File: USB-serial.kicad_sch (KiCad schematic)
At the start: 14 parts

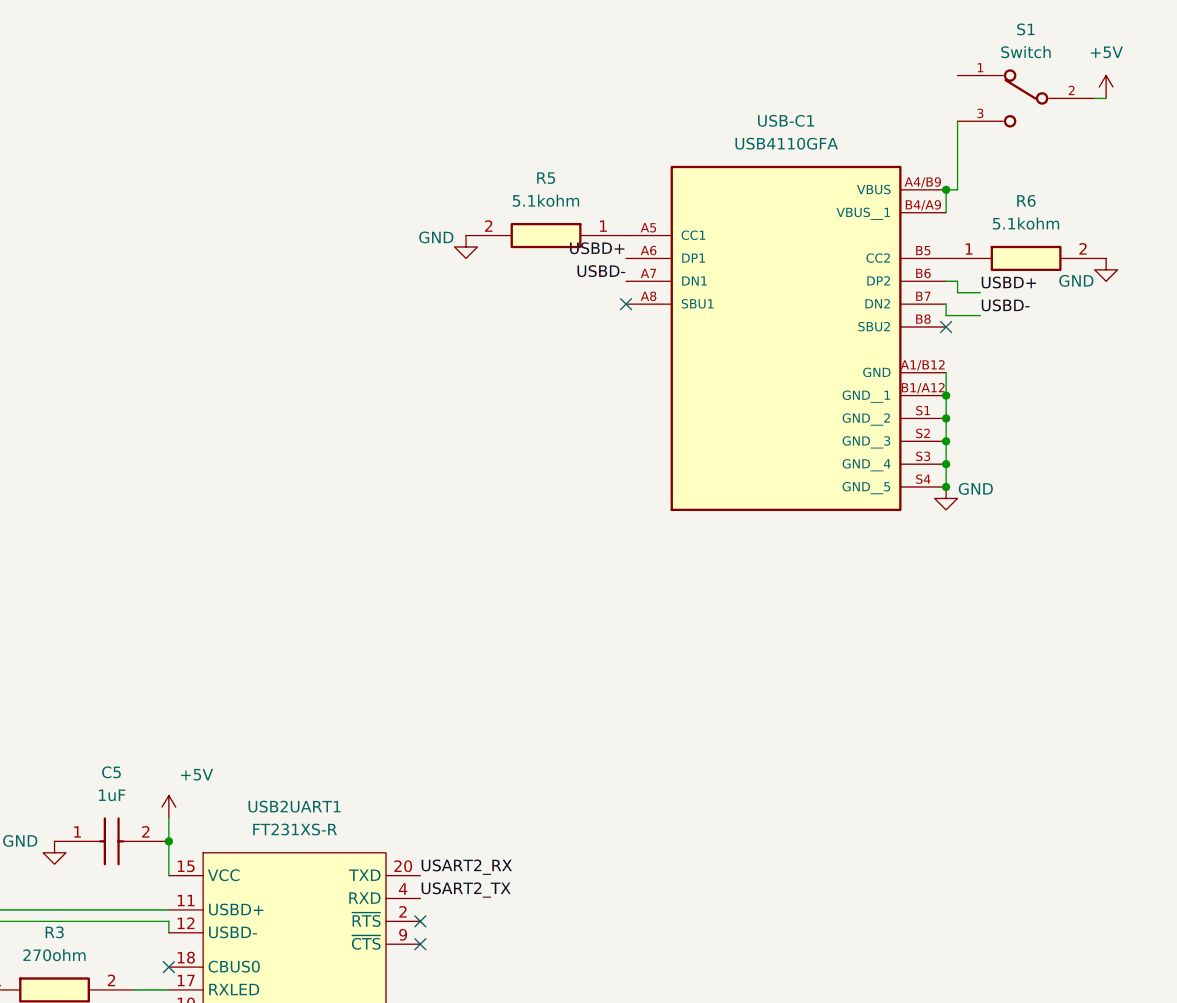
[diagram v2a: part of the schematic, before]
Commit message: standardize 5V and 3V3 labels
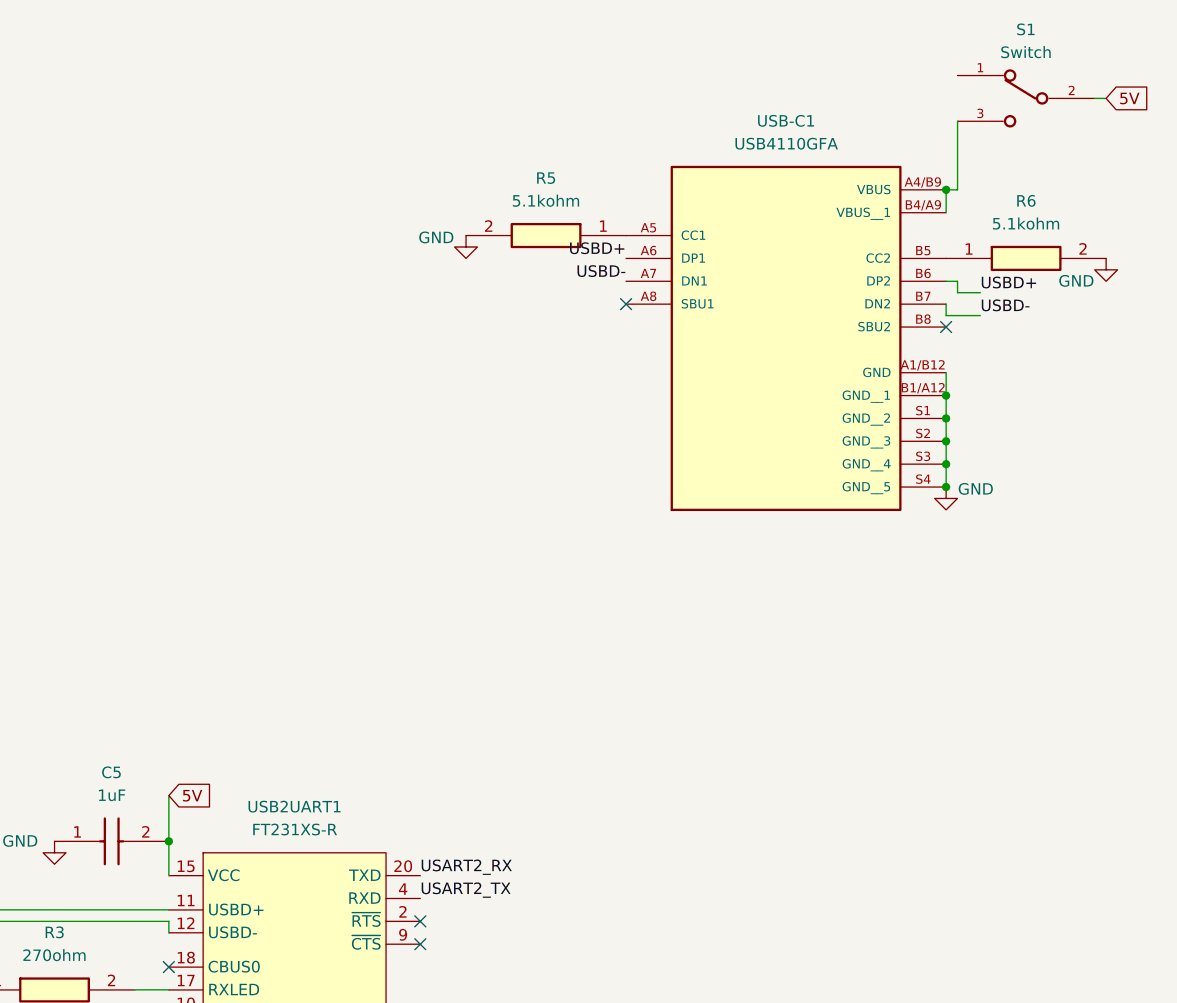
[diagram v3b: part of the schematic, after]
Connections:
- net +5V renamed 5V
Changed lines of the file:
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@@
 	(wire
 		(pts
-			(xy 102.87 139.7) (xy 102.87 142.24)
+			(xy 102.87 137.16) (xy 102.87 142.24)
 		)
 		(stroke
@@
 			)
 			(justify right bottom)
+		)
+	)
+	(global_label "5V"
+		(shape input)
+		(at 102.87 137.16 0)
+		(fields_autoplaced yes)
+		(effects
+			(font
+				(size 1.27 1.27)
+			)
+			(justify left)
+		)
+		(property "Intersheetrefs" "${INTERSHEET_REFS}"
+			(at 108.1533 137.16 0)
+			(effects
+				(font
+					(size 1.27 1.27)
+				)
+				(justify left)
+				(hide yes)
+			)
+		)
+	)
+	(global_label "5V"
+		(shape input)
+		(at 207.01 59.69 0)
+		(fields_autoplaced yes)
+		(effects
+			(font
+				(size 1.27 1.27)
+			)
+			(justify left)
+		)
+		(property "Intersheetrefs" "${INTERSHEET_REFS}"
+			(at 212.2933 59.69 0)
+			(effects
+				(font
+					(size 1.27 1.27)
+				)
+				(justify left)
+				(hide yes)
+			)
 		)
 	)
@@
 	)
 	(symbol
-		(lib_id "power:+5V")
-		(at 207.01 59.69 0)
-		(mirror y)
-		(unit 1)
-		(exclude_from_sim no)
-		(in_bom yes)
-		(on_board yes)
-		(dnp no)
-		(property "Reference" "#PWR012"
-			(at 207.01 63.5 0)
-			(effects
-				(font
-					(size 1.27 1.27)
-				)
-				(hide yes)
-			)
-		)
-		(property "Value" "+5V"
-			(at 207.01 54.61 0)
-			(effects
-				(font
-					(size 1.27 1.27)
-				)
-			)
-		)
-		(property "Footprint" ""
-			(at 207.01 59.69 0)
-			(effects
-				(font
-					(size 1.27 1.27)
-				)
-				(hide yes)
-			)
-		)
-		(property "Datasheet" ""
-			(at 207.01 59.69 0)
-			(effects
-				(font
-					(size 1.27 1.27)
-				)
-				(hide yes)
-			)
-		)
-		(property "Description" "Power symbol creates a global label with name \"+5V\""
-			(at 207.01 59.69 0)
-			(effects
-				(font
-					(size 1.27 1.27)
-				)
-				(hide yes)
-			)
-		)
-		(pin "1"
-		)
-		(instances
-			(project "harm_drone"
-				(path "/5ce3566e-4e0f-420e-9b0d-3952cd3c63fd/8f41fec2-6210-43dd-9328-85befbc13075"
-					(reference "#PWR012")
-					(unit 1)
-				)
-			)
-		)
-	)
-	(symbol
 		(lib_id "power:GND")
 		(at 207.01 77.47 0)
@@
 					(unit 1)
 				)
-			)
-		)
-	)
-	(symbol
-		(lib_id "power:+5V")
-		(at 102.87 139.7 0)
-		(mirror y)
-		(unit 1)
-		(exclude_from_sim no)
-		(in_bom yes)
-		(on_board yes)
-		(dnp no)
-		(property "Reference" "#PWR09"
-			(at 102.87 143.51 0)
-			(effects
-				(font
-					(size 1.27 1.27)
-				)
-				(hide yes)
-			)
-		)
-		(property "Value" "+5V"
-			(at 105.918 134.874 0)
-			(effects
-				(font
-					(size 1.27 1.27)
-				)
-			)
-		)
-		(property "Footprint" ""
-			(at 102.87 139.7 0)
-			(effects
-				(font
-					(size 1.27 1.27)
-				)
-				(hide yes)
-			)
-		)
-		(property "Datasheet" ""
-			(at 102.87 139.7 0)
-			(effects
-				(font
-					(size 1.27 1.27)
-				)
-				(hide yes)
-			)
-		)
-		(property "Description" "Power symbol creates a global label with name \"+5V\""
-			(at 102.87 139.7 0)
-			(effects
-				(font
-					(size 1.27 1.27)
-				)
-				(hide yes)
-			)
-		)
-		(pin "1"
-		)
-		(instances
-			(project "harm_drone"
-				(path "/5ce3566e-4e0f-420e-9b0d-3952cd3c63fd/8f41fec2-6210-43dd-9328-85befbc13075"
-					(reference "#PWR09")
-					(unit 1)
-				)

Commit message: finished up schematic
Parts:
- renumbered C3 to C12, C4 to C13, C5 to C14, R1 to R10, R2 to R11, R3 to R12, R4 to R13, R5 to R14, R6 to R15, S1 to S2
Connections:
- net USART2_RX renamed TXD_USB2SERIAL
- net USART2_TX renamed RXD_USB2SERIAL
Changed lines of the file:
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@@
+	(wire
+		(pts
+			(xy 134.62 146.05) (xy 130.81 146.05)
+		)
+		(stroke
+			(width 0)
+			(type default)
+		)
+	)
 	(wire
 		(pts
@@
 		(pts
 			(xy 193.04 83.82) (xy 189.23 83.82)
+		)
+		(stroke
+			(width 0)
+			(type default)
+		)
+	)
+	(wire
+		(pts
+			(xy 133.35 148.59) (xy 130.81 148.59)
 		)
 		(stroke
@@
 		)
 	)
-	(label "USART2_RX"
-		(at 130.81 146.05 0)
-		(fields_autoplaced yes)
-		(effects
-			(font
-				(size 1.27 1.27)
-			)
-			(justify left bottom)
-		)
-	)
 	(label "USBD-"
 		(at 153.67 80.01 180)
@@
 		)
 	)
-	(label "USART2_TX"
-		(at 130.81 148.59 0)
-		(fields_autoplaced yes)
-		(effects
-			(font
-				(size 1.27 1.27)
-			)
-			(justify left bottom)
-		)
-	)
 	(label "VCCIO"
 		(at 133.35 165.1 0)
@@
 			)
 			(justify right bottom)
+		)
+	)
+	(global_label "RXD_USB2SERIAL"
+		(shape input)
+		(at 133.35 148.59 0)
+		(effects
+			(font
+				(size 1.27 1.27)
+			)
+			(justify left)
+		)
+		(property "Intersheetrefs" "${INTERSHEET_REFS}"
+			(at 133.35 148.59 0)
+			(effects
+				(font
+					(size 1.27 1.27)
+				)
+				(hide yes)
+			)
+		)
+	)
+	(global_label "TXD_USB2SERIAL"
+		(shape output)
+		(at 134.62 146.05 0)
+		(effects
+			(font
+				(size 1.27 1.27)
+			)
+			(justify left)
+		)
+		(property "Intersheetrefs" "${INTERSHEET_REFS}"
+			(at 134.62 146.05 0)
+			(effects
+				(font
+					(size 1.27 1.27)
+				)
+				(hide yes)
+			)
 		)
 	)
@@
 		(on_board yes)
 		(dnp no)
-		(property "Reference" "#PWR08"
+		(property "Reference" "#PWR029"
 			(at 90.17 148.59 0)
 			(effects
@@
 			(project "harm_drone"
 				(path "/5ce3566e-4e0f-420e-9b0d-3952cd3c63fd/8f41fec2-6210-43dd-9328-85befbc13075"
-					(reference "#PWR08")
+					(reference "#PWR029")
 					(unit 1)
 				)
@@
 		(dnp no)
 		(fields_autoplaced yes)
-		(property "Reference" "R4"
+		(property "Reference" "R13"
 			(at 90.17 168.91 0)
 			(effects
@@
 			(project "harm_drone"
 				(path "/5ce3566e-4e0f-420e-9b0d-3952cd3c63fd/8f41fec2-6210-43dd-9328-85befbc13075"
-					(reference "R4")
+					(reference "R13")
 					(unit 1)
 				)
@@
 		(dnp no)
 		(fields_autoplaced yes)
-		(property "Reference" "S1"
+		(property "Reference" "S2"
 			(at 198.12 52.07 0)
 			(effects
@@
 			(project ""
 				(path "/5ce3566e-4e0f-420e-9b0d-3952cd3c63fd/8f41fec2-6210-43dd-9328-85befbc13075"
-					(reference "S1")
+					(reference "S2")
 					(unit 1)
 				)
@@
 		(dnp no)
 		(fields_autoplaced yes)
-		(property "Reference" "C5"
+		(property "Reference" "C14"
 			(at 96.52 134.62 0)
 			(effects
@@
 			(project "harm_drone"
 				(path "/5ce3566e-4e0f-420e-9b0d-3952cd3c63fd/8f41fec2-6210-43dd-9328-85befbc13075"
-					(reference "C5")
+					(reference "C14")
 					(unit 1)
 				)
@@
 		(on_board yes)
 		(dnp no)
-		(property "Reference" "#PWR013"
+		(property "Reference" "#PWR032"
 			(at 189.23 109.22 0)
 			(effects
@@
 			(project "harm_drone"
 				(path "/5ce3566e-4e0f-420e-9b0d-3952cd3c63fd/8f41fec2-6210-43dd-9328-85befbc13075"
-					(reference "#PWR013")
+					(reference "#PWR032")
 					(unit 1)
 				)
@@
 		(on_board yes)
 		(dnp no)
-		(property "Reference" "#PWR010"
+		(property "Reference" "#PWR031"
 			(at 135.89 81.28 0)
 			(effects
@@
 			(project "harm_drone"
 				(path "/5ce3566e-4e0f-420e-9b0d-3952cd3c63fd/8f41fec2-6210-43dd-9328-85befbc13075"
-					(reference "#PWR010")
+					(reference "#PWR031")
 					(unit 1)
 				)
@@
 		(on_board yes)
 		(dnp no)
-		(property "Reference" "#PWR06"
+		(property "Reference" "#PWR027"
 			(at 50.8 156.21 0)
 			(effects
@@
 			(project "harm_drone"
 				(path "/5ce3566e-4e0f-420e-9b0d-3952cd3c63fd/8f41fec2-6210-43dd-9328-85befbc13075"
-					(reference "#PWR06")
+					(reference "#PWR027")
 					(unit 1)
 				)
@@
 		(dnp no)
 		(fields_autoplaced yes)
-		(property "Reference" "R6"
+		(property "Reference" "R15"
 			(at 198.12 71.12 0)
 			(effects
@@
 			(project "harm_drone"
 				(path "/5ce3566e-4e0f-420e-9b0d-3952cd3c63fd/8f41fec2-6210-43dd-9328-85befbc13075"
-					(reference "R6")
+					(reference "R15")
 					(unit 1)
 				)
@@
 		(on_board yes)
 		(dnp no)
-		(property "Reference" "#PWR011"
+		(property "Reference" "#PWR030"
 			(at 130.81 184.15 0)
 			(effects
@@
 			(project "harm_drone"
 				(path "/5ce3566e-4e0f-420e-9b0d-3952cd3c63fd/8f41fec2-6210-43dd-9328-85befbc13075"
-					(reference "#PWR011")
+					(reference "#PWR030")
 					(unit 1)
 				)
@@
 		(dnp no)
 		(fields_autoplaced yes)
-		(property "Reference" "R2"
+		(property "Reference" "R11"
 			(at 71.12 128.27 0)
 			(effects
@@
 			(project "harm_drone"
 				(path "/5ce3566e-4e0f-420e-9b0d-3952cd3c63fd/8f41fec2-6210-43dd-9328-85befbc13075"
-					(reference "R2")
+					(reference "R11")
 					(unit 1)
 				)
@@
 		(dnp no)
 		(fields_autoplaced yes)
-		(property "Reference" "R1"
+		(property "Reference" "R10"
 			(at 69.85 139.7 0)
 			(effects
@@
 			(project "harm_drone"
 				(path "/5ce3566e-4e0f-420e-9b0d-3952cd3c63fd/8f41fec2-6210-43dd-9328-85befbc13075"
-					(reference "R1")
+					(reference "R10")
 					(unit 1)
 				)
@@
 		(on_board yes)
 		(dnp no)
-		(property "Reference" "#PWR014"
+		(property "Reference" "#PWR033"
 			(at 207.01 83.82 0)
 			(effects
@@
 			(project "harm_drone"
 				(path "/5ce3566e-4e0f-420e-9b0d-3952cd3c63fd/8f41fec2-6210-43dd-9328-85befbc13075"
-					(reference "#PWR014")
+					(reference "#PWR033")
 					(unit 1)
 				)
@@
 		(dnp no)
 		(fields_autoplaced yes)
-		(property "Reference" "R3"
+		(property "Reference" "R12"
 			(at 90.17 152.4 0)
 			(effects
@@
 			(project "harm_drone"
 				(path "/5ce3566e-4e0f-420e-9b0d-3952cd3c63fd/8f41fec2-6210-43dd-9328-85befbc13075"
-					(reference "R3")
+					(reference "R12")
 					(unit 1)
 				)
@@
 		(dnp no)
 		(fields_autoplaced yes)
-		(property "Reference" "C3"
+		(property "Reference" "C12"
 			(at 54.61 142.2399 90)
 			(effects
@@
 			(project "harm_drone"
 				(path "/5ce3566e-4e0f-420e-9b0d-3952cd3c63fd/8f41fec2-6210-43dd-9328-85befbc13075"
-					(reference "C3")
+					(reference "C12")
 					(unit 1)
 				)
@@
 		(dnp no)
 		(fields_autoplaced yes)
-		(property "Reference" "R5"
+		(property "Reference" "R14"
 			(at 144.78 68.58 0)
 			(effects
@@
 			(project "harm_drone"
 				(path "/5ce3566e-4e0f-420e-9b0d-3952cd3c63fd/8f41fec2-6210-43dd-9328-85befbc13075"
-					(reference "R5")
+					(reference "R14")
 					(unit 1)
 				)
@@
 		(dnp no)
 		(fields_autoplaced yes)
-		(property "Reference" "C4"
+		(property "Reference" "C13"
 			(at 55.88 126.9999 90)
 			(effects
@@
 			(project "harm_drone"
 				(path "/5ce3566e-4e0f-420e-9b0d-3952cd3c63fd/8f41fec2-6210-43dd-9328-85befbc13075"
-					(reference "C4")
+					(reference "C13")
 					(unit 1)
 				)
@@
 		(on_board yes)
 		(dnp no)
-		(property "Reference" "#PWR07"
+		(property "Reference" "#PWR028"
 			(at 52.07 115.57 0)
 			(effects
@@
 			(project "harm_drone"
 				(path "/5ce3566e-4e0f-420e-9b0d-3952cd3c63fd/8f41fec2-6210-43dd-9328-85befbc13075"
-					(reference "#PWR07")
+					(reference "#PWR028")
 					(unit 1)
 				)

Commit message: final changes
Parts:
- renumbered C12 to C27, C13 to C28, C14 to C29, R10 to R25, R11 to R26, R12 to R27, R13 to R28, R14 to R29, R15 to R30
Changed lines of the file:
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@@
 		(on_board yes)
 		(dnp no)
-		(property "Reference" "#PWR029"
+		(property "Reference" "#PWR034"
 			(at 90.17 148.59 0)
 			(effects
@@
 			(project "harm_drone"
 				(path "/5ce3566e-4e0f-420e-9b0d-3952cd3c63fd/8f41fec2-6210-43dd-9328-85befbc13075"
-					(reference "#PWR029")
+					(reference "#PWR034")
 					(unit 1)
 				)
@@
 		(dnp no)
 		(fields_autoplaced yes)
-		(property "Reference" "R13"
+		(property "Reference" "R28"
 			(at 90.17 168.91 0)
 			(effects
@@
 			(project "harm_drone"
 				(path "/5ce3566e-4e0f-420e-9b0d-3952cd3c63fd/8f41fec2-6210-43dd-9328-85befbc13075"
-					(reference "R13")
+					(reference "R28")
 					(unit 1)
 				)
@@
 		(dnp no)
 		(fields_autoplaced yes)
-		(property "Reference" "C14"
+		(property "Reference" "C29"
 			(at 96.52 134.62 0)
 			(effects
@@
 			(project "harm_drone"
 				(path "/5ce3566e-4e0f-420e-9b0d-3952cd3c63fd/8f41fec2-6210-43dd-9328-85befbc13075"
-					(reference "C14")
+					(reference "C29")
 					(unit 1)
 				)
@@
 		(on_board yes)
 		(dnp no)
-		(property "Reference" "#PWR032"
+		(property "Reference" "#PWR037"
 			(at 189.23 109.22 0)
 			(effects
@@
 			(project "harm_drone"
 				(path "/5ce3566e-4e0f-420e-9b0d-3952cd3c63fd/8f41fec2-6210-43dd-9328-85befbc13075"
-					(reference "#PWR032")
+					(reference "#PWR037")
 					(unit 1)
 				)
@@
 		(on_board yes)
 		(dnp no)
-		(property "Reference" "#PWR031"
+		(property "Reference" "#PWR036"
 			(at 135.89 81.28 0)
 			(effects
@@
 			(project "harm_drone"
 				(path "/5ce3566e-4e0f-420e-9b0d-3952cd3c63fd/8f41fec2-6210-43dd-9328-85befbc13075"
-					(reference "#PWR031")
+					(reference "#PWR036")
 					(unit 1)
 				)
@@
 		(on_board yes)
 		(dnp no)
-		(property "Reference" "#PWR027"
+		(property "Reference" "#PWR032"
 			(at 50.8 156.21 0)
 			(effects
@@
 			(project "harm_drone"
 				(path "/5ce3566e-4e0f-420e-9b0d-3952cd3c63fd/8f41fec2-6210-43dd-9328-85befbc13075"
-					(reference "#PWR027")
+					(reference "#PWR032")
 					(unit 1)
 				)
@@
 		(dnp no)
 		(fields_autoplaced yes)
-		(property "Reference" "R15"
+		(property "Reference" "R30"
 			(at 198.12 71.12 0)
 			(effects
@@
 			(project "harm_drone"
 				(path "/5ce3566e-4e0f-420e-9b0d-3952cd3c63fd/8f41fec2-6210-43dd-9328-85befbc13075"
-					(reference "R15")
+					(reference "R30")
 					(unit 1)
 				)
@@
 		(on_board yes)
 		(dnp no)
-		(property "Reference" "#PWR030"
+		(property "Reference" "#PWR035"
 			(at 130.81 184.15 0)
 			(effects
@@
 			(project "harm_drone"
 				(path "/5ce3566e-4e0f-420e-9b0d-3952cd3c63fd/8f41fec2-6210-43dd-9328-85befbc13075"
-					(reference "#PWR030")
+					(reference "#PWR035")
 					(unit 1)
 				)
@@
 		(dnp no)
 		(fields_autoplaced yes)
-		(property "Reference" "R11"
+		(property "Reference" "R26"
 			(at 71.12 128.27 0)
 			(effects
@@
 			(project "harm_drone"
 				(path "/5ce3566e-4e0f-420e-9b0d-3952cd3c63fd/8f41fec2-6210-43dd-9328-85befbc13075"
-					(reference "R11")
+					(reference "R26")
 					(unit 1)
 				)
@@
 		(dnp no)
 		(fields_autoplaced yes)
-		(property "Reference" "R10"
+		(property "Reference" "R25"
 			(at 69.85 139.7 0)
 			(effects
@@
 			(project "harm_drone"
 				(path "/5ce3566e-4e0f-420e-9b0d-3952cd3c63fd/8f41fec2-6210-43dd-9328-85befbc13075"
-					(reference "R10")
+					(reference "R25")
 					(unit 1)
 				)
@@
 		(on_board yes)
 		(dnp no)
-		(property "Reference" "#PWR033"
+		(property "Reference" "#PWR038"
 			(at 207.01 83.82 0)
 			(effects
@@
 			(project "harm_drone"
 				(path "/5ce3566e-4e0f-420e-9b0d-3952cd3c63fd/8f41fec2-6210-43dd-9328-85befbc13075"
-					(reference "#PWR033")
+					(reference "#PWR038")
 					(unit 1)
 				)
@@
 		(dnp no)
 		(fields_autoplaced yes)
-		(property "Reference" "R12"
+		(property "Reference" "R27"
 			(at 90.17 152.4 0)
 			(effects
@@
 			(project "harm_drone"
 				(path "/5ce3566e-4e0f-420e-9b0d-3952cd3c63fd/8f41fec2-6210-43dd-9328-85befbc13075"
-					(reference "R12")
+					(reference "R27")
 					(unit 1)
 				)
@@
 		(dnp no)
 		(fields_autoplaced yes)
-		(property "Reference" "C12"
+		(property "Reference" "C27"
 			(at 54.61 142.2399 90)
 			(effects
@@
 			(project "harm_drone"
 				(path "/5ce3566e-4e0f-420e-9b0d-3952cd3c63fd/8f41fec2-6210-43dd-9328-85befbc13075"
-					(reference "C12")
+					(reference "C27")
 					(unit 1)
 				)
@@
 		(dnp no)
 		(fields_autoplaced yes)
-		(property "Reference" "R14"
+		(property "Reference" "R29"
 			(at 144.78 68.58 0)
 			(effects
@@
 			(project "harm_drone"
 				(path "/5ce3566e-4e0f-420e-9b0d-3952cd3c63fd/8f41fec2-6210-43dd-9328-85befbc13075"
-					(reference "R14")
+					(reference "R29")
 					(unit 1)
 				)
@@
 		(dnp no)
 		(fields_autoplaced yes)
-		(property "Reference" "C13"
+		(property "Reference" "C28"
 			(at 55.88 126.9999 90)
 			(effects
@@
 			(project "harm_drone"
 				(path "/5ce3566e-4e0f-420e-9b0d-3952cd3c63fd/8f41fec2-6210-43dd-9328-85befbc13075"
-					(reference "C13")
+					(reference "C28")
 					(unit 1)
 				)
@@
 		(on_board yes)
 		(dnp no)
-		(property "Reference" "#PWR028"
+		(property "Reference" "#PWR033"
 			(at 52.07 115.57 0)
 			(effects
@@
 			(project "harm_drone"
 				(path "/5ce3566e-4e0f-420e-9b0d-3952cd3c63fd/8f41fec2-6210-43dd-9328-85befbc13075"
-					(reference "#PWR028")
+					(reference "#PWR033")
 					(unit 1)
 				)

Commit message: USB stack changes
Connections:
- net 5V: no longer C29.2, USB2UART1.15 (VCC)
- net at S2.3, USB-C1.A4/B9 (VBUS), USB-C1.B4/A9 (VBUS__1): now also C29.2, USB2UART1.15 (VCC)

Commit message: final changes to 3d models
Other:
- moved on the sheet: C27, C28, C29, R25, R26, R27, R28, RXLED1, TXLED1, USB2UART1
